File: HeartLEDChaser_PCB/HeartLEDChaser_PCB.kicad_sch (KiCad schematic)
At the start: 34 parts, among them U1 ICM7555CBAZ, U2 CD4017BM, U3 HT7733A, U4 HX SS12F44G4

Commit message: Routed PCB
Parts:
- H1: footprint MountingHole:MountingHole_2.7mm -> MountingHole:MountingHole_2.1mm
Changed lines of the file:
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@@
 			)
 		)
-		(property "Footprint" "MountingHole:MountingHole_2.7mm"
+		(property "Footprint" "MountingHole:MountingHole_2.1mm"
 			(at 16.51 149.86 0)
 			(effects

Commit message: Improved layout & routing
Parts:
- removed C2: 47nF, FOOTPRINTS:C85925, symbol Device:C
- removed U3: HT7733A, FOOTPRINTS:HT7733A, symbol HT7733A:HT7733A
- added U3: HT7750A, FOOTPRINTS:HT7750A, symbol HT7750A:HT7750A_C259884
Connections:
- net GND: now also U1.5 (CONTROL_VOLTAGE), U3.4 (GND); no longer R7.2
- net at U2.5 (6): now also D5.2 (A); no longer D7.2 (A)
- net at R7.1: no longer D5.1 (K)
- net at D1.2 (A): now also U2.1 (5); no longer U2.3 (0)
- net at D8.2 (A): now also U2.9 (8); no longer U2.6 (7)
- net at D6.2 (A): now also U2.6 (7); no longer U2.1 (5)
- net at D9.2 (A): now also U2.10 (4); no longer U2.9 (8)
- net at D3.2 (A): now also U2.3 (0); no longer U2.4 (2)
- net at D4.2 (A): now also U2.4 (2); no longer U2.7 (3)
- net at L1.2, S1.2 (A): now also U3.5 (LX)
- net +3V3 renamed +5V
- net +5V: now also U3.1 (CE), U3.2 (VOUT)
- new net: D7.2 (A), U2.7 (3)
- no-connect marks 5 -> 6
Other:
- moved on the sheet: BT1, C3, C4, H1, L1, S1, U4

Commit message: Cleanup
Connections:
- net GND: now also R7.1
- net at R7.2: now also D5.1 (K)
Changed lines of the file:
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@@
 	)
 	(junction
+		(at 100.33 83.82)
+		(diameter 0)
+		(color 0 0 0 0)
+	)
+	(junction
 		(at 72.39 170.18)
 		(diameter 0)
@@
 	(wire
 		(pts
-			(xy 100.33 81.28) (xy 100.33 86.36)
+			(xy 100.33 81.28) (xy 100.33 83.82)
 		)
 		(stroke
@@
 	(wire
 		(pts
+			(xy 100.33 83.82) (xy 100.33 86.36)
+		)
+		(stroke
+			(width 0)
+			(type default)
+		)
+	)
+	(wire
+		(pts
 			(xy 93.98 26.67) (xy 95.25 26.67)
 		)
@@
 	(symbol
 		(lib_id "Device:R")
-		(at 96.52 83.82 180)
+		(at 96.52 83.82 270)
 		(unit 1)
 		(exclude_from_sim no)
@@
 		(fields_autoplaced yes)
 		(property "Reference" "R7"
-			(at 90.17 83.82 90)
+			(at 96.52 90.17 90)
 			(effects
 				(font
@@
 		)
 		(property "Value" "3.3k"
-			(at 92.71 83.82 90)
+			(at 96.52 87.63 90)
 			(effects
 				(font
@@
 		)
 		(property "Footprint" "FOOTPRINTS:0402WGJ0332TCE"
-			(at 98.298 83.82 90)
+			(at 96.52 82.042 90)
 			(effects
 				(font

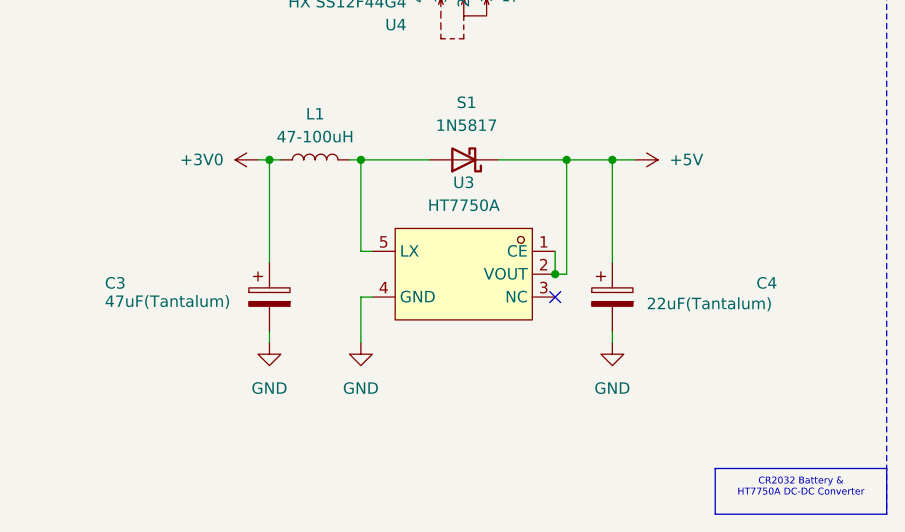
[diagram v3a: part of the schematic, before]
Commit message: Corrected capacitor references
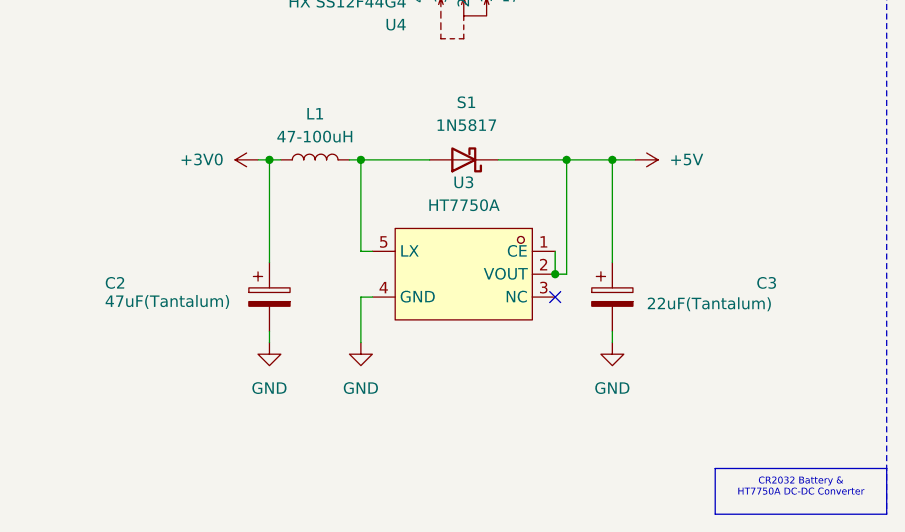
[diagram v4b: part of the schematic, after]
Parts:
- renumbered C3 to C2, C4 to C3
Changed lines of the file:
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@@
 		(on_board yes)
 		(dnp no)
-		(property "Reference" "C3"
+		(property "Reference" "C2"
 			(at 22.352 171.196 0)
 			(effects
@@
 			(project ""
 				(path "/407f145c-340e-4b78-9c61-323751cc61f8"
-					(reference "C3")
+					(reference "C2")
 					(unit 1)
 				)
@@
 		(on_board yes)
 		(dnp no)
-		(property "Reference" "C4"
+		(property "Reference" "C3"
 			(at 94.742 171.196 0)
 			(effects
@@
 			(project ""
 				(path "/407f145c-340e-4b78-9c61-323751cc61f8"
-					(reference "C4")
-					(unit 1)
-				)
+					(reference "C3")
+					(unit 1)
+				)
